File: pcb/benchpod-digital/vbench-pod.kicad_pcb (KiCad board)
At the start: 4 copper layers, 98.5 x 120.2 mm, 325 parts, among them CN1 KH-FPC1.0-H2.0SMT-24P-QCHF, J1 X9555WR-2x13-6TV01, J10 Conn_02x02_Counter_Clockwise, J11 Conn_02x02_Counter_Clockwise, J4 DB2ERC-3.81-2P-BK, J5 DB2ERC-3.81-2P-BK, J6 DB2ERC-3.81-2P-BK, J7 HR911105A_C12074, SW1 TS24CA, SW2 TS24CA, U1 ICE40UP5K-SG48ITR, U10 TCAN1044VDRBRQ1, U18 SN74LVC2G66DCUR, U19 SN74LVC2G66DCUR, U2 W25Q64JVSSIQ, U20 SN74LVC2G66DCUR, U21 SN74LVC2G66DCUR, U22 SRV05-4.TCT, U23 SRV05-4.TCT, U24 SN74LVC2G66DCUR, U25 SRV05-4.TCT, U26 TPS259470ARPWR, U27 TPS259470ARPWR, U28 SRV05-4.TCT, U29 INA226AIDGSR, U30 TPS62130ARGTR, U31 AP2112K-1.2, U32 AP2112K-2.5TRG1, U33 INA226AIDGSR, U34 SRV05-4.TCT, U35 INA226AIDGSR, U5 STM32H563ZGT6, U52 AP2112K-1.8TRG1, U54 TCA9554PWR, U56 TCA9554PWR, U57 TPS259470ARPWR, U59 SY6280AAC, U6 LAN8742AI-CZ-TR, U60 SY6280AAC, U7 APS6404L-3SQR-SN, U8 TPS2116DRLR, X1 SX3M48.000B10F20TNN, Y1 6pF ±10ppm SMD2016-4P Crystal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, Y2 6pF ±10ppm SMD2016-4P Crystal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

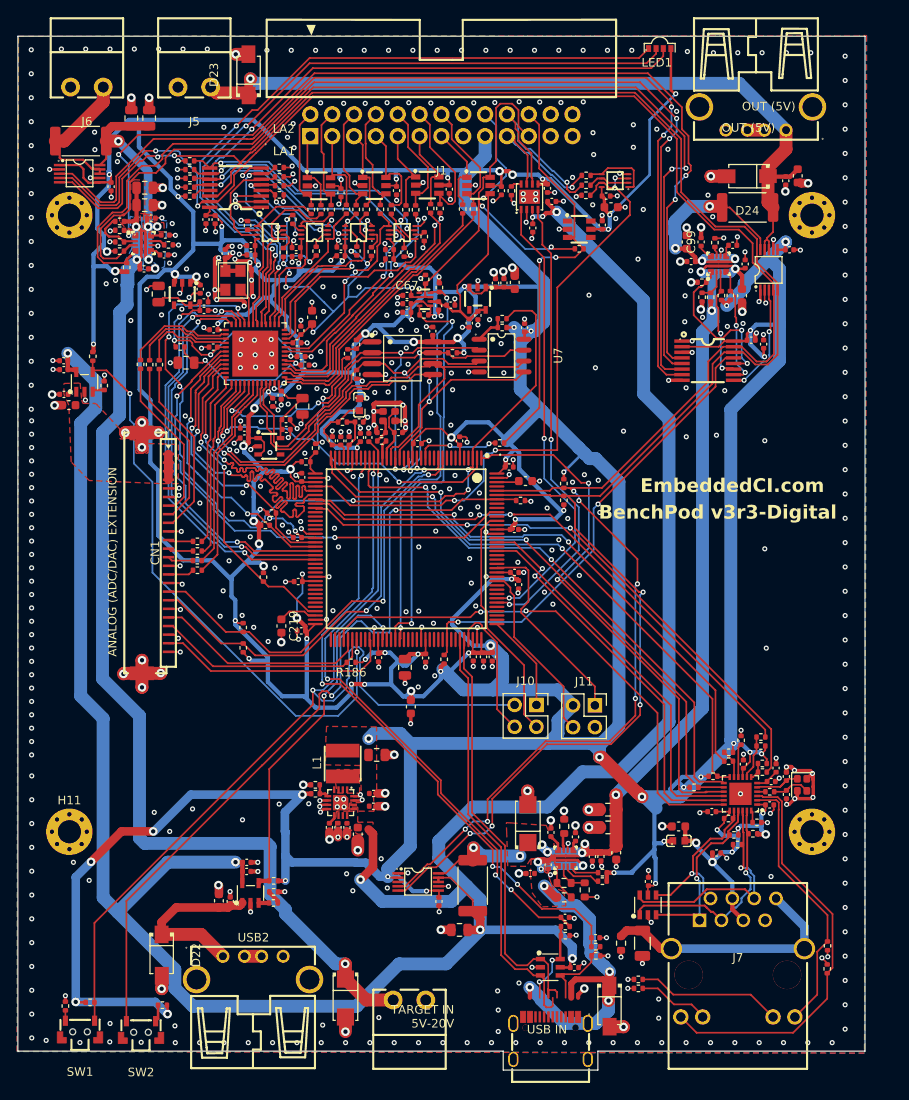
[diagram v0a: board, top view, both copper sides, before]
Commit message: fixes for enclosure
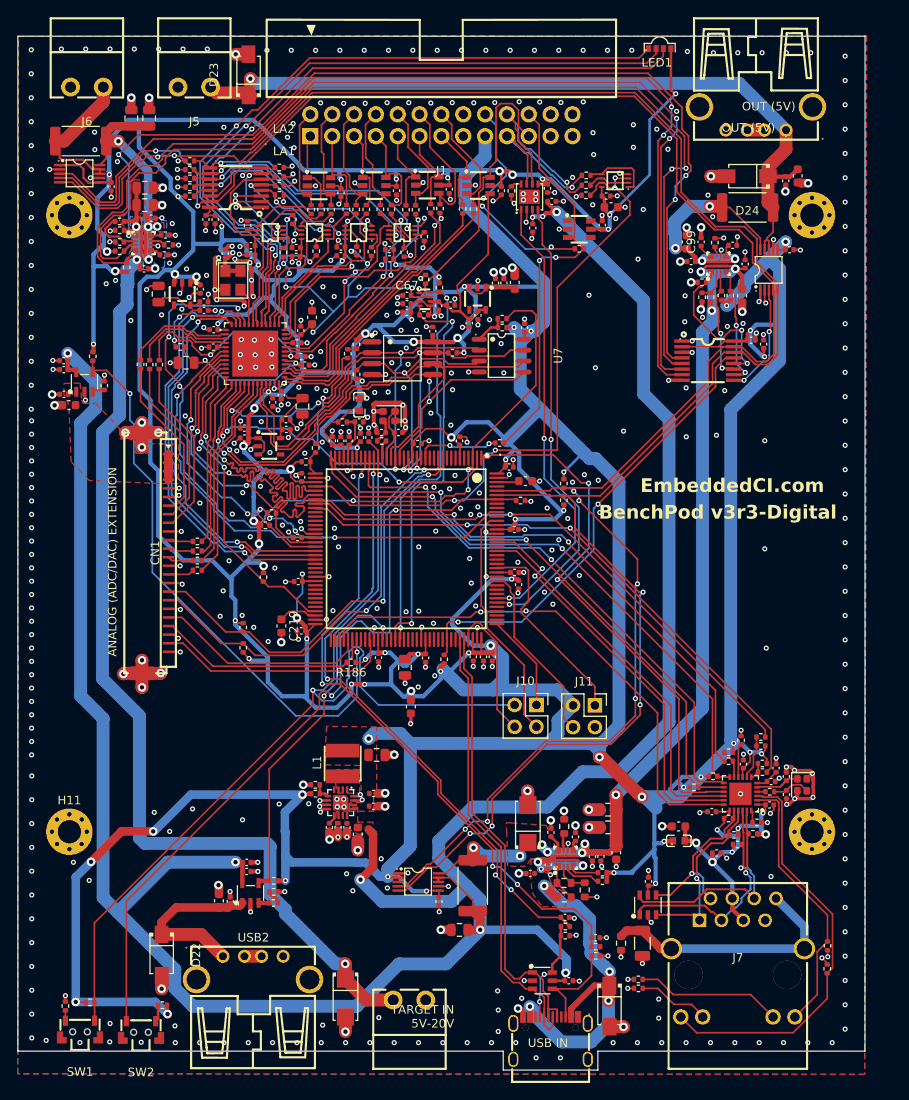
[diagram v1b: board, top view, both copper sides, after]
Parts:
- moved D11 1.81 mm to (118.0, 125.1)
- moved C245 1.67 mm to (121.1, 125.1)
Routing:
- net /USB/USB_CC2: track 9.28 -> 13.1 mm
- net /P_USB_D-: track 50.0 -> 52.5 mm
- net /P_USB_D+: track 50.9 -> 53.1 mm
- net /USB/USB_CC1: track 9.83 -> 12.0 mm
- net +5V_EFUSE: track 51.3 -> 53.3 mm
- net +5V: track 306.9 -> 308.3 mm
- net GND: track 301.6 -> 301.5 mm, vias 606 -> 605
